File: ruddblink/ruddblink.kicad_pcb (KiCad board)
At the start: 2 copper layers, 40.6 x 48.5 mm, 30 parts, among them Q1 IRFML8244, SW1 JS202011JCQN, SW2 PTS526 SK15 SMTR2 LFS, U1 ATtiny85-20SU, U2 74HC595

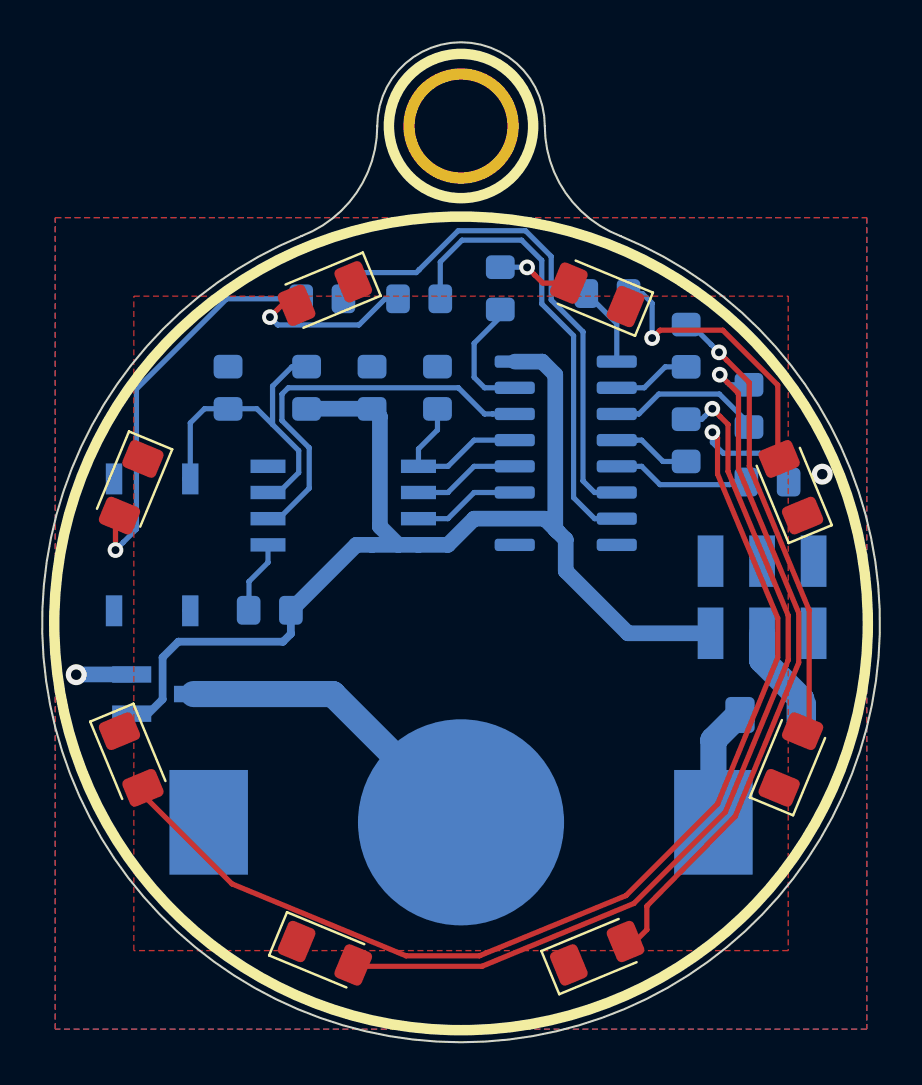
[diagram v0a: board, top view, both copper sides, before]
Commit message: Adjust some positions and shrink soldermask clearance
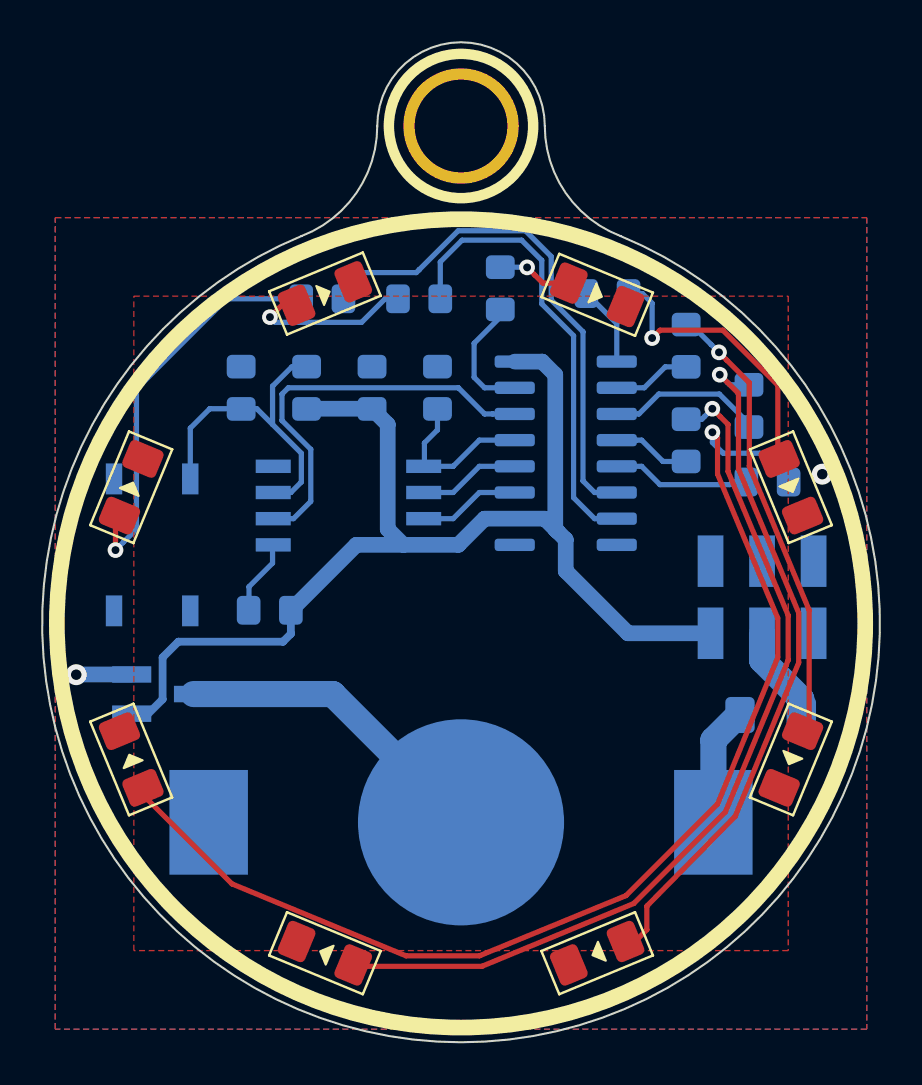
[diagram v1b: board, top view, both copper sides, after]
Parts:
- D1, D2, D3, D4, D5, D6, D7, D8: footprint LED_SMD:LED_1206_3216Metric_Pad1.42x1.75mm_HandSolder -> ruddblink:LED_1206_Uniform_HandSolder
- moved C3 0.63 mm to (131.6, 102.9)
- moved G*** 0.40 mm to (142.4, 114.6)
- moved U1 0.25 mm to (136.8, 108.6)
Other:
- rule pad_to_mask_clearance: 0.2 -> 0.0508
- rule solder_mask_min_width: 0.25 -> 0.1016
- board text added: "v0"
- board text removed: "v0.1"

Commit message: Reposition some designators
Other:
- board text added: "NEG"
- board text removed: "CENT NEG"
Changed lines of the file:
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@@
   (general
     (thickness 1.6)
-    (drawings 46)
+    (drawings 48)
     (tracks 212)
     (zones 0)
@@
     (tags "Keystone type 3034 coin cell retainer")
     (attr smd)
-    (fp_text reference BT1 (at 15.24 -0.762 90) (layer B.SilkS)
+    (fp_text reference BT1 (at -11.557 4.445 90) (layer B.SilkS)
       (effects (font (size 1 1) (thickness 0.15)) (justify mirror))
     )
@@
     (tags SOT-23)
     (attr smd)
-    (fp_text reference Q1 (at 1.905 -1.524) (layer B.SilkS)
+    (fp_text reference Q1 (at 2.032 -1.524) (layer B.SilkS)
       (effects (font (size 1 1) (thickness 0.15)) (justify mirror))
     )
@@
     (tags "resistor handsolder")
     (attr smd)
-    (fp_text reference F1 (at -3.5925 -1.651) (layer B.SilkS)
+    (fp_text reference F1 (at -3.3385 -1.651) (layer B.SilkS)
       (effects (font (size 1 1) (thickness 0.15)) (justify mirror))
     )
@@
     )
   )
+  (gr_circle (center 130.429 120.142) (end 130.556 120.142) (layer B.SilkS) (width 0.254))
+  (gr_circle (center 130.429 120.142) (end 129.921 120.269) (layer B.SilkS) (width 0.15))
   (gr_circle (center 142.24 114.3) (end 129.54 114.3) (layer Dwgs.User) (width 0.15))
   (gr_circle (center 142.24 114.3) (end 129.54 123.19) (layer Dwgs.User) (width 0.15))
@@
     (effects (font (size 1.397 1.397) (thickness 0.254)) (justify mirror))
   )
-  (gr_text "CENT NEG" (at 128.016 120.269) (layer B.SilkS)
-    (effects (font (size 0.8128 0.8128) (thickness 0.1016)) (justify mirror))
+  (gr_text NEG (at 128.27 120.269) (layer B.SilkS)
+    (effects (font (size 0.8128 0.8128) (thickness 0.1524)) (justify mirror))
   )
   (gr_text + (at 158.115 121.92) (layer B.SilkS)

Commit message: Vanity edits
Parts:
- moved U1 0.38 mm to (137.2, 108.6)
- moved SW1 0.13 mm to (156.7, 113.0)
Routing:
- net /SER: track 20.2 -> 20.8 mm
